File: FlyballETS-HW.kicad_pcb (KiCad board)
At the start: 2 copper layers, 94 x 108 mm, 62 parts, among them J1 CONN_01X03, J10 CONN_01X03, J11 CONN_01X03, J12 CONN_01X03, J13 CONN_01X03, J14 CONN_01X03, J15 CONN_01X03, J16 CONN_01X03, J17 CONN_01X03, J18 CONN_01X03, J19 CONN_01X03, J2 CONN_01X03, J20 CONN_01X03, J21 CONN_01X02, J22 CONN_01X02, J23 CONN_01X02, J24 CONN_01X03, J25 CONN_02X09, J26 CONN_01X08, J27 CONN_01X02, J28 Conn_01x04, J29 CONN_01X03, J3 CONN_01X03, J4 CONN_01X03, J5 CONN_01X03, J6 CONN_01X03, J7 CONN_01X03, J8 CONN_01X03, J9 CONN_01X03, Q1 BC557, Q2 BC557, U1 Wemos_LoLin32, U2 DC-DCStepdown-LM2596

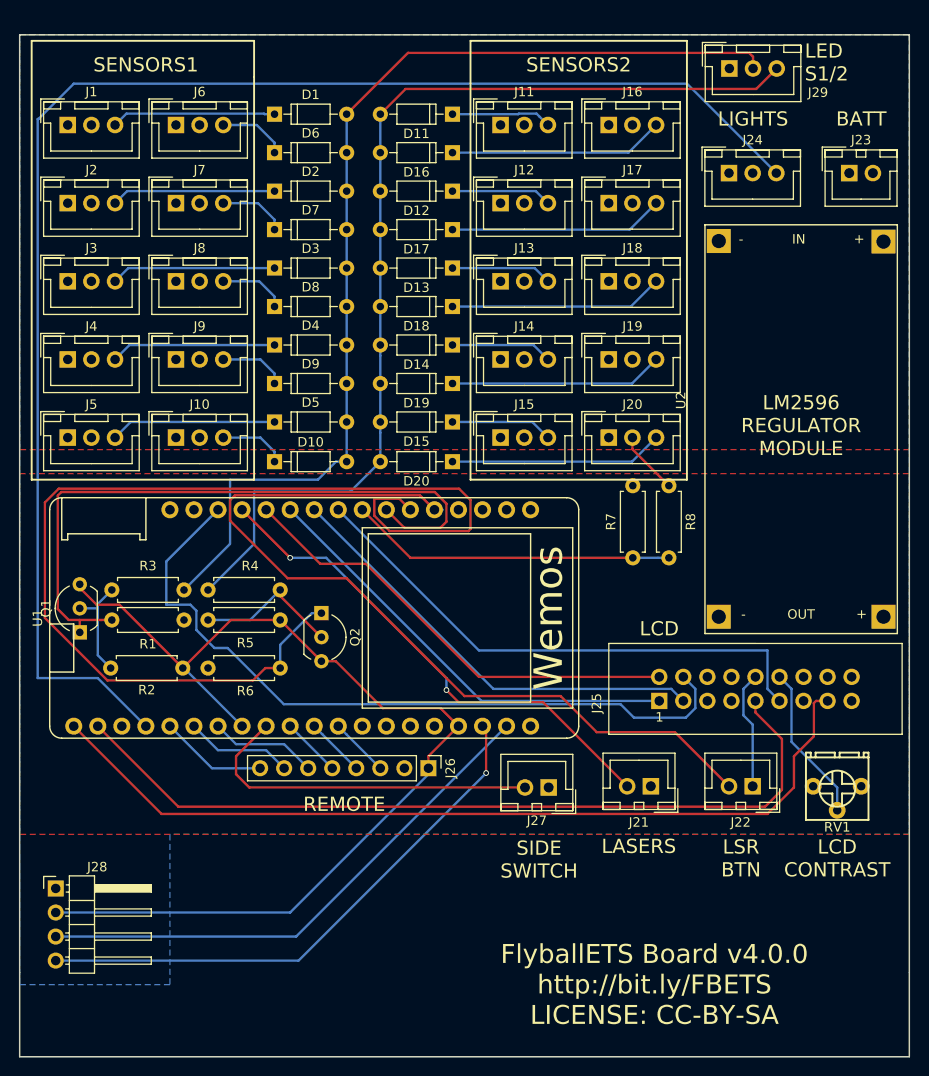
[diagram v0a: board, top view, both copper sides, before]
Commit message: Corrected GPS connections
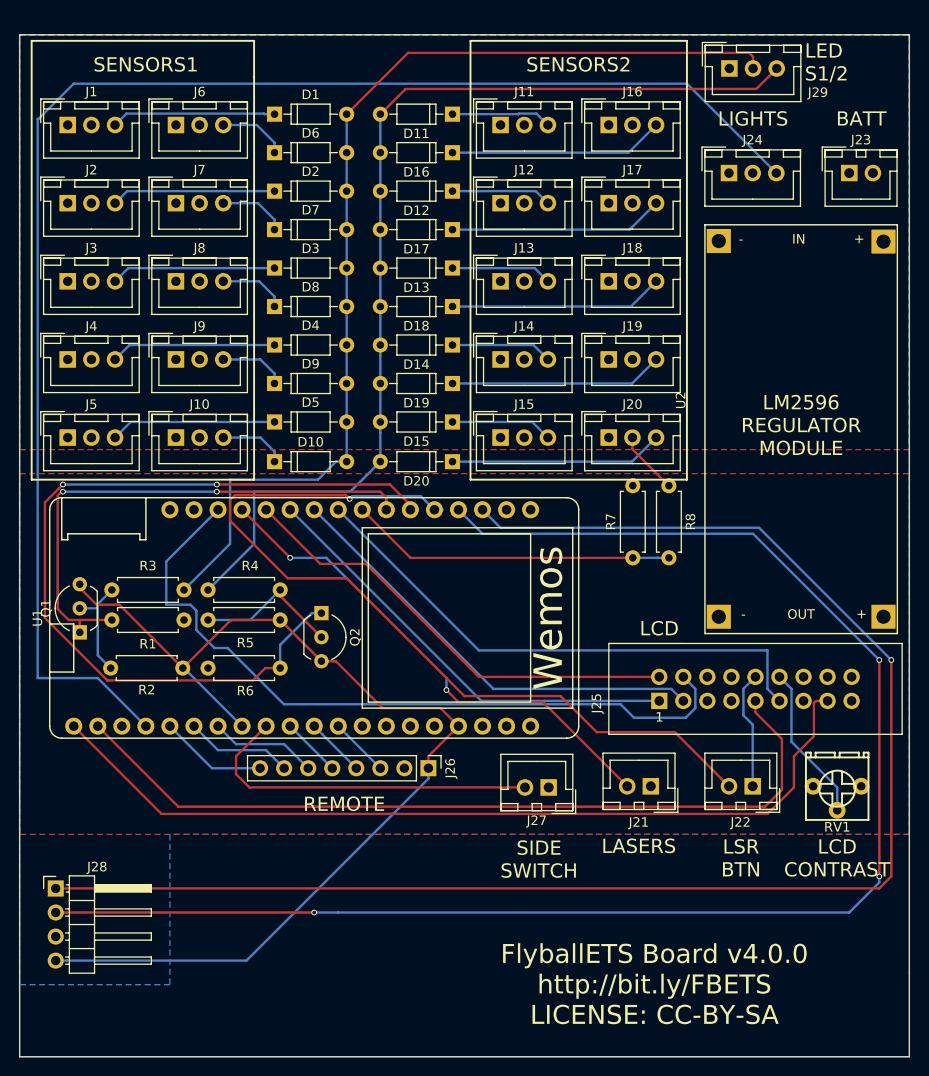
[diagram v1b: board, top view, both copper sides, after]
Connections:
- J28 pad 1: GND -> GPSRX
- J28 pad 2: +3V3 -> GPSTX
- J28 pad 3: GPSRX -> GND
- J28 pad 4: GPSTX -> +3V3
- U1 pad 18: GPSRX -> Net-(U1-Pad18)
- U1 pad 19: GPSTX -> Net-(U1-Pad19)
- U1 pad 3: Net-(U1-Pad3) -> GPSRX
- U1 pad 4: Net-(U1-Pad4) -> GPSTX
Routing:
- net GPSRX: track 56.8 -> 161.4 mm, vias 0 -> 1
- net GPSTX: track 58.8 -> 162.8 mm, vias 1 -> 3
- net S2-IN: track 114.6 -> 89.3 mm, vias 0 -> 2
- net S1-IN: track 71.0 -> 57.0 mm, vias 0 -> 2
- net +3V3: track 111.4 -> 114.4 mm
- net Net-(U1-Pad19): track 0.00 -> 0.54 mm
- net LSRBTN: track 89.8 -> 90.0 mm, vias 0 -> 1

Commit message: Fixed smaller issues
- Added mounting holes
- Added 1000uF cap for Ws2811 lights
- Added 300R resistor in WS2811 data line
- Removed  transistors to invert sensor signal (we need to use NPN, NO from now on)
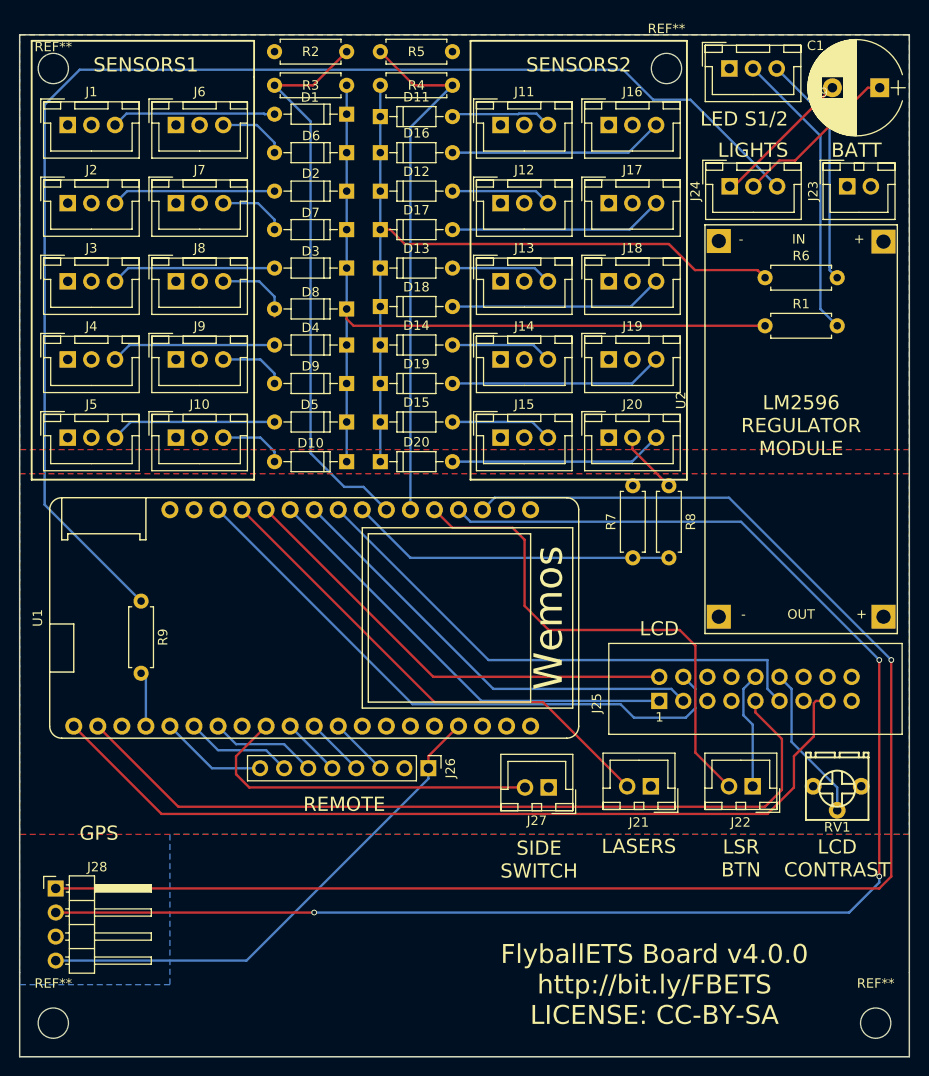
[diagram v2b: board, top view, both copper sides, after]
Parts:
- removed Q1, Q2: BC557, TO_SOT_Packages_THT:TO-92_Inline_Wide
- added C1: 1000uF, Capacitors_THT:CP_Radial_D10.0mm_P5.00mm, F.Cu at (156.9, 39.9)
- added R9: 300, Resistors_THT:R_Axial_DIN0207_L6.3mm_D2.5mm_P7.62mm_Horizontal, F.Cu at (78.9, 94.1)
- added REF**: MountingHole_3.2mm_M3, Mounting_Holes:MountingHole_3.2mm_M3, F.Cu at (69.6, 37.8)
- added REF**: MountingHole_3.2mm_M3, Mounting_Holes:MountingHole_3.2mm_M3, F.Cu at (69.6, 138.7)
- added REF**: MountingHole_3.2mm_M3, Mounting_Holes:MountingHole_3.2mm_M3, F.Cu at (134.4, 37.8)
- added REF**: MountingHole_3.2mm_M3, Mounting_Holes:MountingHole_3.2mm_M3, F.Cu at (156.5, 138.7)
- R1, R6: value 4k7 -> 500
- R2, R5: value 1k -> 300
- R3, R4: value 2k2 -> 1k
- moved R6 71.8 mm to (144.8, 59.9)
- moved R1 68.8 mm to (144.8, 65.0), turned to 0 degrees
- moved R2 65.8 mm to (93.0, 36.1), turned to 0 degrees
- moved R5 62.7 mm to (111.8, 36.1)
- moved R4 56.3 mm to (111.8, 39.6)
- moved R3 56.0 mm to (93.0, 39.6)
- moved D11 7.62 mm to (104.1, 42.9), turned to 0 degrees
- moved D8 7.62 mm to (100.6, 63.2), turned to 180 degrees
- moved D1 7.62 mm to (100.6, 42.7), turned to 180 degrees
- moved D10 7.62 mm to (100.6, 79.4), turned to 180 degrees
- moved D12 7.62 mm to (104.1, 50.8), turned to 0 degrees
- moved D13 7.62 mm to (104.1, 58.9), turned to 0 degrees
- moved D14 7.62 mm to (104.1, 67.1), turned to 0 degrees
- moved D15 7.62 mm to (104.1, 75.2), turned to 0 degrees
- moved D16 7.62 mm to (104.1, 46.7), turned to 0 degrees
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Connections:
- D1 pad 1: Net-(D1-Pad1) -> S1
- D1 pad 2: S1 -> Net-(D1-Pad2)
- D10 pad 1: Net-(D10-Pad1) -> S1
- D10 pad 2: S1 -> Net-(D10-Pad2)
- D11 pad 1: Net-(D11-Pad1) -> S2
- D11 pad 2: S2 -> Net-(D11-Pad2)
- D12 pad 1: Net-(D12-Pad1) -> S2
- D12 pad 2: S2 -> Net-(D12-Pad2)
- D13 pad 1: Net-(D13-Pad1) -> S2
- D13 pad 2: S2 -> Net-(D13-Pad2)
- D14 pad 1: Net-(D14-Pad1) -> S2
- D14 pad 2: S2 -> Net-(D14-Pad2)
- D15 pad 1: Net-(D15-Pad1) -> S2
- D15 pad 2: S2 -> Net-(D15-Pad2)
- D16 pad 1: Net-(D16-Pad1) -> S2
- D16 pad 2: S2 -> Net-(D16-Pad2)
- D17 pad 1: Net-(D17-Pad1) -> S2
- D17 pad 2: S2 -> Net-(D17-Pad2)
- D18 pad 1: Net-(D18-Pad1) -> S2
- D18 pad 2: S2 -> Net-(D18-Pad2)
- D19 pad 1: Net-(D19-Pad1) -> S2
- D19 pad 2: S2 -> Net-(D19-Pad2)
- D2 pad 1: Net-(D2-Pad1) -> S1
- D2 pad 2: S1 -> Net-(D2-Pad2)
- D20 pad 1: Net-(D20-Pad1) -> S2
- D20 pad 2: S2 -> Net-(D20-Pad2)
- D3 pad 1: Net-(D3-Pad1) -> S1
- D3 pad 2: S1 -> Net-(D3-Pad2)
- D4 pad 1: Net-(D4-Pad1) -> S1
- D4 pad 2: S1 -> Net-(D4-Pad2)
- D5 pad 1: Net-(D5-Pad1) -> S1
- D5 pad 2: S1 -> Net-(D5-Pad2)
- D6 pad 1: Net-(D6-Pad1) -> S1
- D6 pad 2: S1 -> Net-(D6-Pad2)
- D7 pad 1: Net-(D7-Pad1) -> S1
- D7 pad 2: S1 -> Net-(D7-Pad2)
- D8 pad 1: Net-(D8-Pad1) -> S1
- D8 pad 2: S1 -> Net-(D8-Pad2)
- D9 pad 1: Net-(D9-Pad1) -> S1
- D9 pad 2: S1 -> Net-(D9-Pad2)
- J1 pad 3: Net-(D1-Pad1) -> Net-(D1-Pad2)
- J10 pad 3: Net-(D10-Pad1) -> Net-(D10-Pad2)
- J11 pad 3: Net-(D11-Pad1) -> Net-(D11-Pad2)
- J12 pad 3: Net-(D12-Pad1) -> Net-(D12-Pad2)
- J13 pad 3: Net-(D13-Pad1) -> Net-(D13-Pad2)
- J14 pad 3: Net-(D14-Pad1) -> Net-(D14-Pad2)
- J15 pad 3: Net-(D15-Pad1) -> Net-(D15-Pad2)
- J16 pad 3: Net-(D16-Pad1) -> Net-(D16-Pad2)
- J17 pad 3: Net-(D17-Pad1) -> Net-(D17-Pad2)
- J18 pad 3: Net-(D18-Pad1) -> Net-(D18-Pad2)
- J19 pad 3: Net-(D19-Pad1) -> Net-(D19-Pad2)
- J2 pad 3: Net-(D2-Pad1) -> Net-(D2-Pad2)
- J20 pad 3: Net-(D20-Pad1) -> Net-(D20-Pad2)
- J24 pad 3: LDATA -> Net-(J24-Pad3)
- J25 pad 16: Net-(J25-Pad16) -> (no net)
- J25 pad 5: Net-(J25-Pad5) -> (no net)
- J25 pad 6: Net-(J25-Pad6) -> (no net)
- J25 pad 7: Net-(J25-Pad7) -> (no net)
- J25 pad 8: Net-(J25-Pad8) -> (no net)
- J29 pad 2: S1 -> Net-(J29-Pad2)
- J29 pad 3: S2 -> Net-(J29-Pad3)
- J3 pad 3: Net-(D3-Pad1) -> Net-(D3-Pad2)
- J4 pad 3: Net-(D4-Pad1) -> Net-(D4-Pad2)
- J5 pad 3: Net-(D5-Pad1) -> Net-(D5-Pad2)
- J6 pad 3: Net-(D6-Pad1) -> Net-(D6-Pad2)
- J7 pad 3: Net-(D7-Pad1) -> Net-(D7-Pad2)
- J8 pad 3: Net-(D8-Pad1) -> Net-(D8-Pad2)
- J9 pad 3: Net-(D9-Pad1) -> Net-(D9-Pad2)
- R1 pad 1: GND -> S1
- R1 pad 2: S1-IN -> Net-(J29-Pad2)
- R2 pad 1: +3V3 -> GND
- R2 pad 2: Net-(Q1-Pad2) -> S1-IN
- R3 pad 1: Net-(Q1-Pad2) -> S1-IN
- R4 pad 1: Net-(Q2-Pad2) -> S2-IN
- R5 pad 1: +3V3 -> GND
- R5 pad 2: Net-(Q2-Pad2) -> S2-IN
- R6 pad 1: GND -> S2
- R6 pad 2: S2-IN -> Net-(J29-Pad3)
- U1 pad 18: Net-(U1-Pad18) -> (no net)
- U1 pad 19: Net-(U1-Pad19) -> (no net)
- U1 pad 2: Net-(U1-Pad2) -> (no net)
- U1 pad 21: Net-(U1-Pad21) -> (no net)
- U1 pad 22: Net-(U1-Pad22) -> (no net)
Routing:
- net LDATA: track 156.1 -> 5.80 mm
- net Net-(J24-Pad3): track 0.00 -> 140.7 mm
- net +3V3: track 114.4 -> 55.0 mm
- net LSRBTN: track 90.0 -> 53.9 mm, vias 1 -> 0
- net S2-IN: track 89.3 -> 56.3 mm, vias 2 -> 0
- net Net-(J29-Pad2): track 0.00 -> 30.9 mm
- net S1: track 110.5 -> 85.3 mm
- net S2: track 107.6 -> 82.5 mm
- net Net-(J29-Pad3): track 0.00 -> 24.7 mm
- net Net-(D16-Pad2): track 0.00 -> 22.7 mm
- net Net-(D16-Pad1): track 22.7 -> 0.00 mm
- net Net-(D17-Pad2): track 0.00 -> 22.7 mm
- net Net-(D17-Pad1): track 22.7 -> 0.00 mm
- net Net-(D18-Pad2): track 0.00 -> 22.6 mm
- net Net-(D18-Pad1): track 22.6 -> 0.00 mm
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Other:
- board text added: "GPS"

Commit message: Final version
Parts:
- R2, R5: value 300 -> 330
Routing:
- net +12V: track 24.3 -> 6.67 mm
- net GND: track 27.6 -> 12.9 mm
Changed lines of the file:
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@@
     (thickness 1.6)
     (drawings 29)
-    (tracks 215)
+    (tracks 208)
     (zones 0)
     (modules 66)
@@
       (effects (font (size 1 1) (thickness 0.15)))
     )
-    (fp_text value 300 (at 3.81 2.31) (layer F.Fab)
+    (fp_text value 330 (at 3.81 2.31) (layer F.Fab)
       (effects (font (size 1 1) (thickness 0.15)))
     )
@@
       (effects (font (size 1 1) (thickness 0.15)))
     )
-    (fp_text value 300 (at 3.81 2.31 180) (layer F.Fab)
+    (fp_text value 330 (at 3.81 2.31 180) (layer F.Fab)
       (effects (font (size 1 1) (thickness 0.15)))
     )
@@
   (segment (start 104.14 62.992) (end 104.14 67.056) (width 0.25) (layer B.Cu) (net 2) (status 30))
   (segment (start 104.14 71.12) (end 104.14 75.184) (width 0.25) (layer B.Cu) (net 2) (status 30))
-  (segment (start 151.892 39.878) (end 141.478 50.292) (width 0.25) (layer F.Cu) (net 3))
-  (segment (start 141.478 50.292) (end 141.05 50.292) (width 0.25) (layer F.Cu) (net 3))
+  (segment (start 141.478 50.292) (end 141.05 50.292) (width 0.25) (layer F.Cu) (net 3) (status 30))
   (segment (start 142.494 106.172) (end 143.47 107.148) (width 0.25) (layer B.Cu) (net 3))
   (segment (start 143.47 107.148) (end 143.47 113.665) (width 0.25) (layer B.Cu) (net 3) (status 20))
   (segment (start 142.494 103.378) (end 142.494 106.172) (width 0.25) (layer B.Cu) (net 3))
   (segment (start 143.764 102.108) (end 142.494 103.378) (width 0.25) (layer B.Cu) (net 3) (status 10))
-  (segment (start 147.955 47.565) (end 146.277 47.565) (width 0.25) (layer F.Cu) (net 4))
-  (segment (start 146.277 47.565) (end 143.55 50.292) (width 0.25) (layer F.Cu) (net 4))
-  (segment (start 156.892 39.878) (end 155.642 39.878) (width 0.25) (layer F.Cu) (net 4))
-  (segment (start 155.642 39.878) (end 147.955 47.565) (width 0.25) (layer F.Cu) (net 4))
   (segment (start 130.77 76.835) (end 130.77 78.065) (width 0.25) (layer F.Cu) (net 4) (status 10))
   (segment (start 130.77 78.065) (end 134.62 81.915) (width 0.25) (layer F.Cu) (net 4) (status 20))
@@
   (segment (start 150.622 44.958) (end 143.51 37.846) (width 0.25) (layer B.Cu) (net 50) (status 20))
   (segment (start 151.5999 58.838898) (end 151.5999 43.4359) (width 0.25) (layer B.Cu) (net 51))
-  (segment (start 151.5872 43.4232) (end 146.01 37.846) (width 0.25) (layer B.Cu) (net 51))
-  (segment (start 151.5999 43.4359) (end 151.5872 43.4232) (width 0.25) (layer B.Cu) (net 51))
+  (segment (start 151.5999 43.4359) (end 146.01 37.846) (width 0.25) (layer B.Cu) (net 51) (status 20))
   (segment (start 151.600001 58.838999) (end 151.5999 58.838898) (width 0.25) (layer B.Cu) (net 51))
-  (segment (start 152.4 59.944) (end 151.600001 59.144001) (width 0.25) (layer B.Cu) (net 51))
+  (segment (start 152.4 59.944) (end 151.600001 59.144001) (width 0.25) (layer B.Cu) (net 51) (status 10))
   (segment (start 151.600001 59.144001) (end 151.600001 58.838999) (width 0.25) (layer B.Cu) (net 51))
   (segment (start 68.6816 41.6814) (end 72.39 37.973) (width 0.25) (layer B.Cu) (net 52))
-  (segment (start 78.867 94.107) (end 68.707 83.947) (width 0.25) (layer B.Cu) (net 52))
+  (segment (start 78.867 94.107) (end 68.6816 83.9216) (width 0.25) (layer B.Cu) (net 52) (status 10))
   (segment (start 68.6816 41.6814) (end 68.6816 83.9216) (width 0.25) (layer B.Cu) (net 52))
-  (segment (start 68.6816 83.9216) (end 68.707 83.947) (width 0.25) (layer B.Cu) (net 52))
   (segment (start 72.39 37.973) (end 129.794 37.973) (width 0.25) (layer B.Cu) (net 52))
   (segment (start 129.794 37.973) (end 132.969 41.148) (width 0.25) (layer B.Cu) (net 52))
   (segment (start 132.969 41.148) (end 136.906 41.148) (width 0.25) (layer B.Cu) (net 52))
-  (segment (start 136.906 41.148) (end 146.05 50.292) (width 0.25) (layer B.Cu) (net 52))
+  (segment (start 136.906 41.148) (end 146.05 50.292) (width 0.25) (layer B.Cu) (net 52) (status 20))
   (zone (net 4) (net_name +12V) (layer F.Cu) (hatch edge 0.508)
     (connect_pads (clearance 0.508))
